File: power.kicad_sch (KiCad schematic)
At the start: 61 parts, among them J7 USB-C_GCT_USB4105-GF-A, J8 Molex_Nano-Fit_1x2_SMD_105430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, U13 TPS564247DRLR, U6 TPS564247DRLR, U7 TPS564247DRLR, U8 TPS564247DRLR, U9 TPS564247DRLR

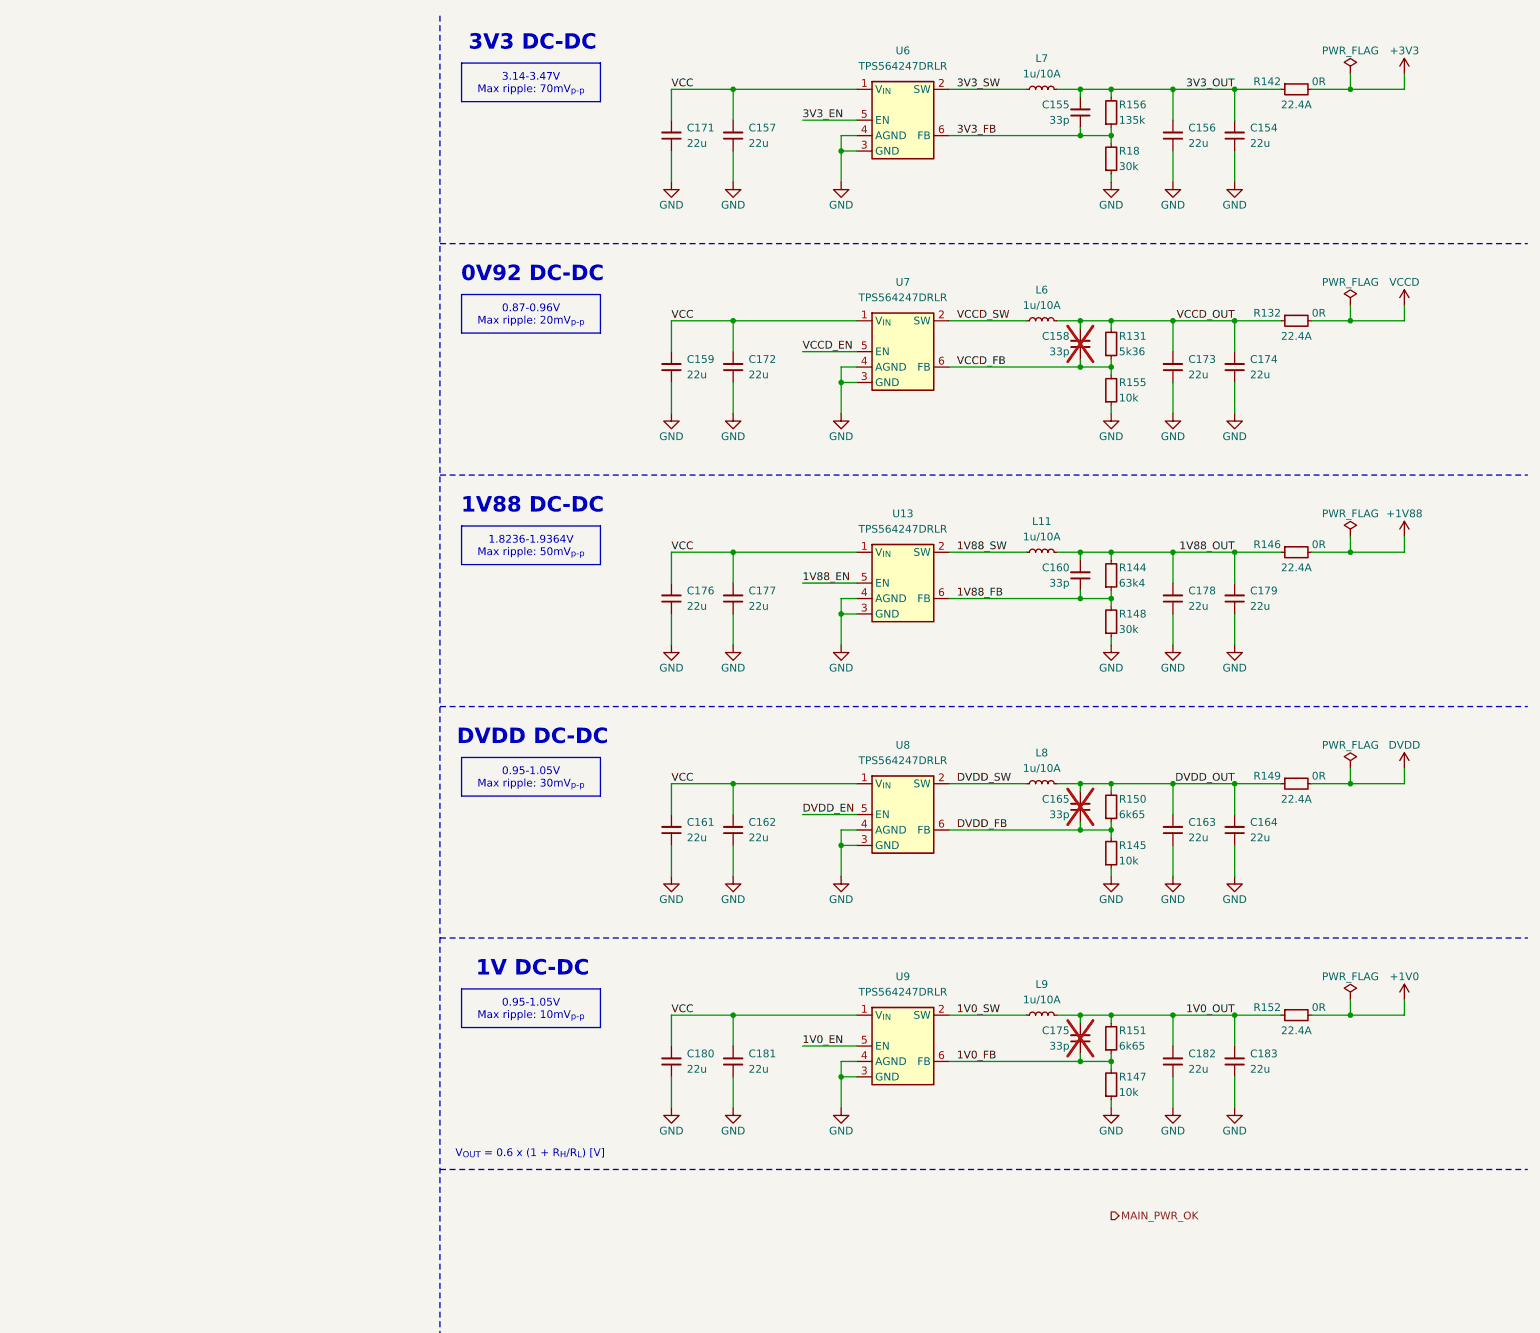
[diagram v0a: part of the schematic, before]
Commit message: [#81595] WIP: Connect remaining control signals
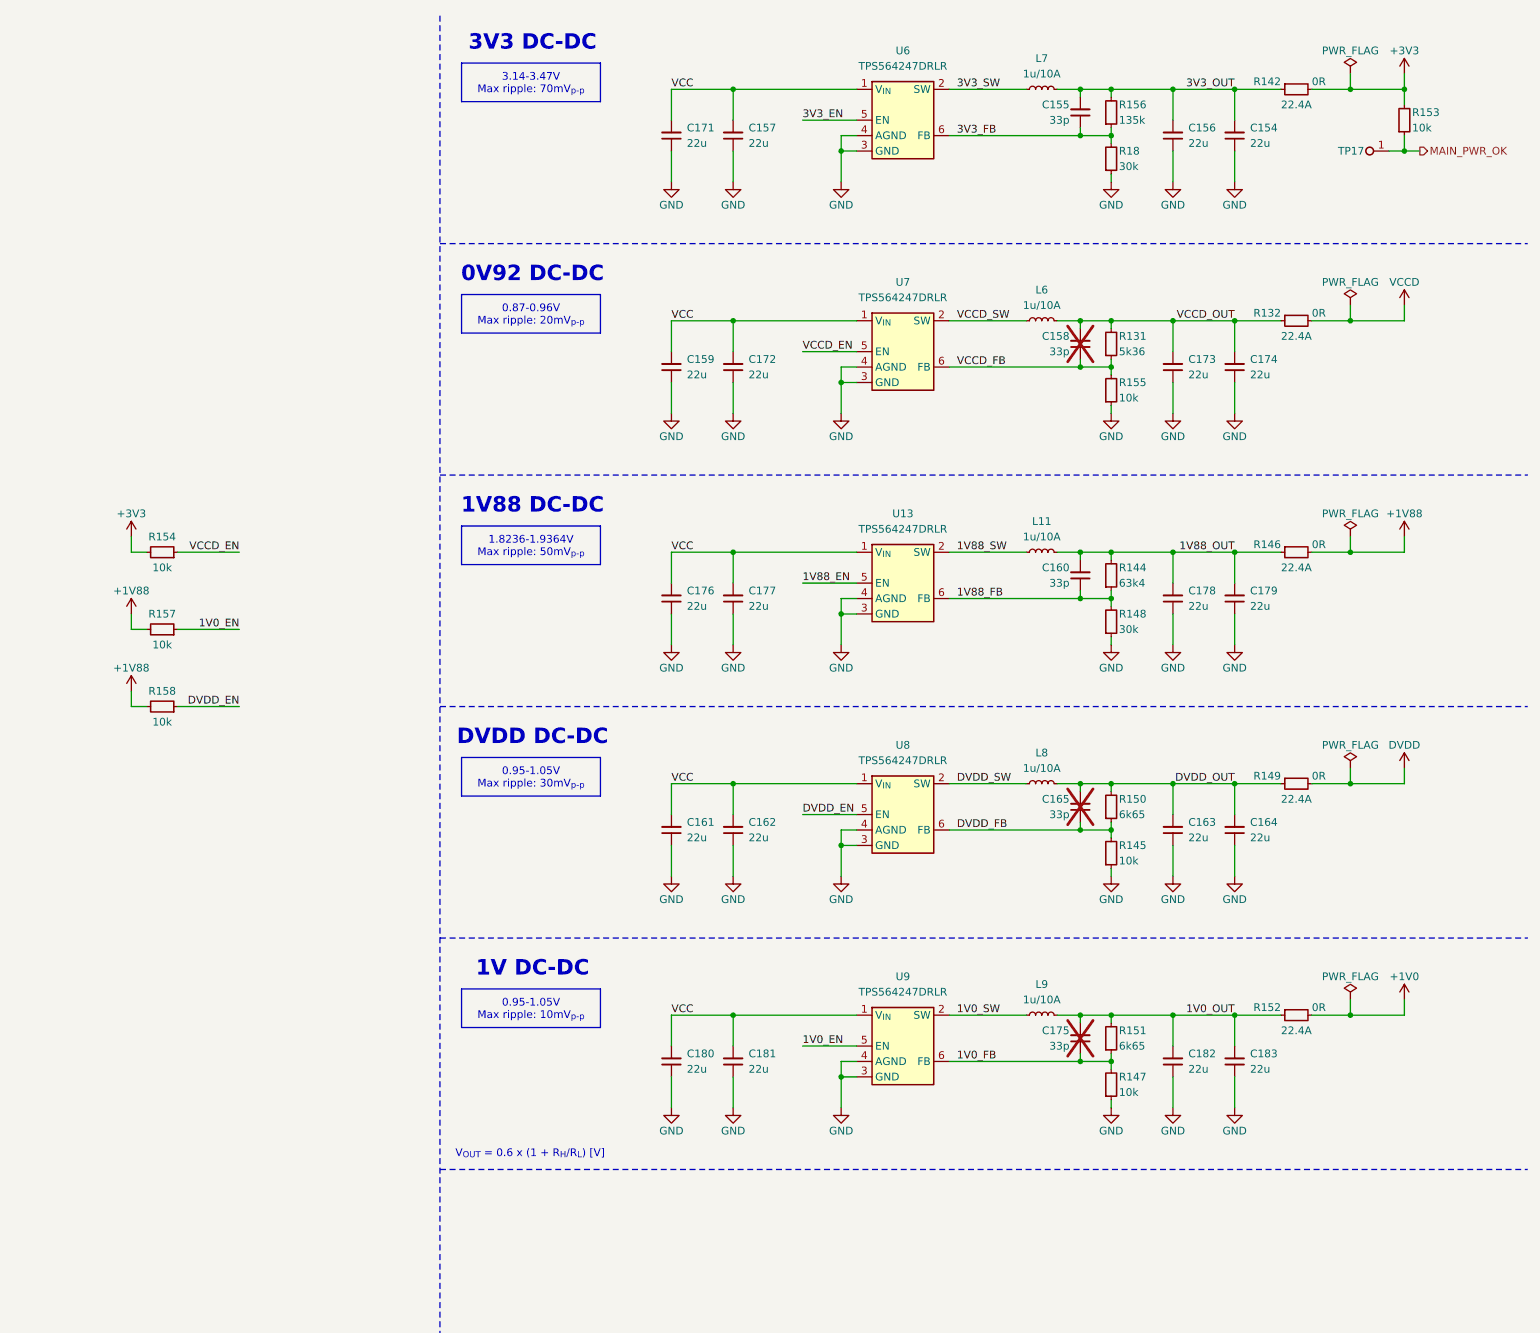
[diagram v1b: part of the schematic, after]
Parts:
- added R153, R154, R157, R158: R_10k_0402, antmicro-footprints:R_0402_1005Metric, symbol antmicroResistors0402:R_10k_0402
- added TP17: TP_0.75mm_SMD, antmicro-footprints:TP_SMD_0.75mm, symbol antmicroTestPoints:TP_0.75mm_SMD
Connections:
- net +1V88: now also R157.2, R158.2
- net +3V3: now also R153.2, R154.2
- net 1V0_EN: now also R157.1
- net DVDD_EN: now also R158.1
- net MAIN_PWR_OK: now also R153.1, TP17.1
- net VCCD_EN: now also R154.1

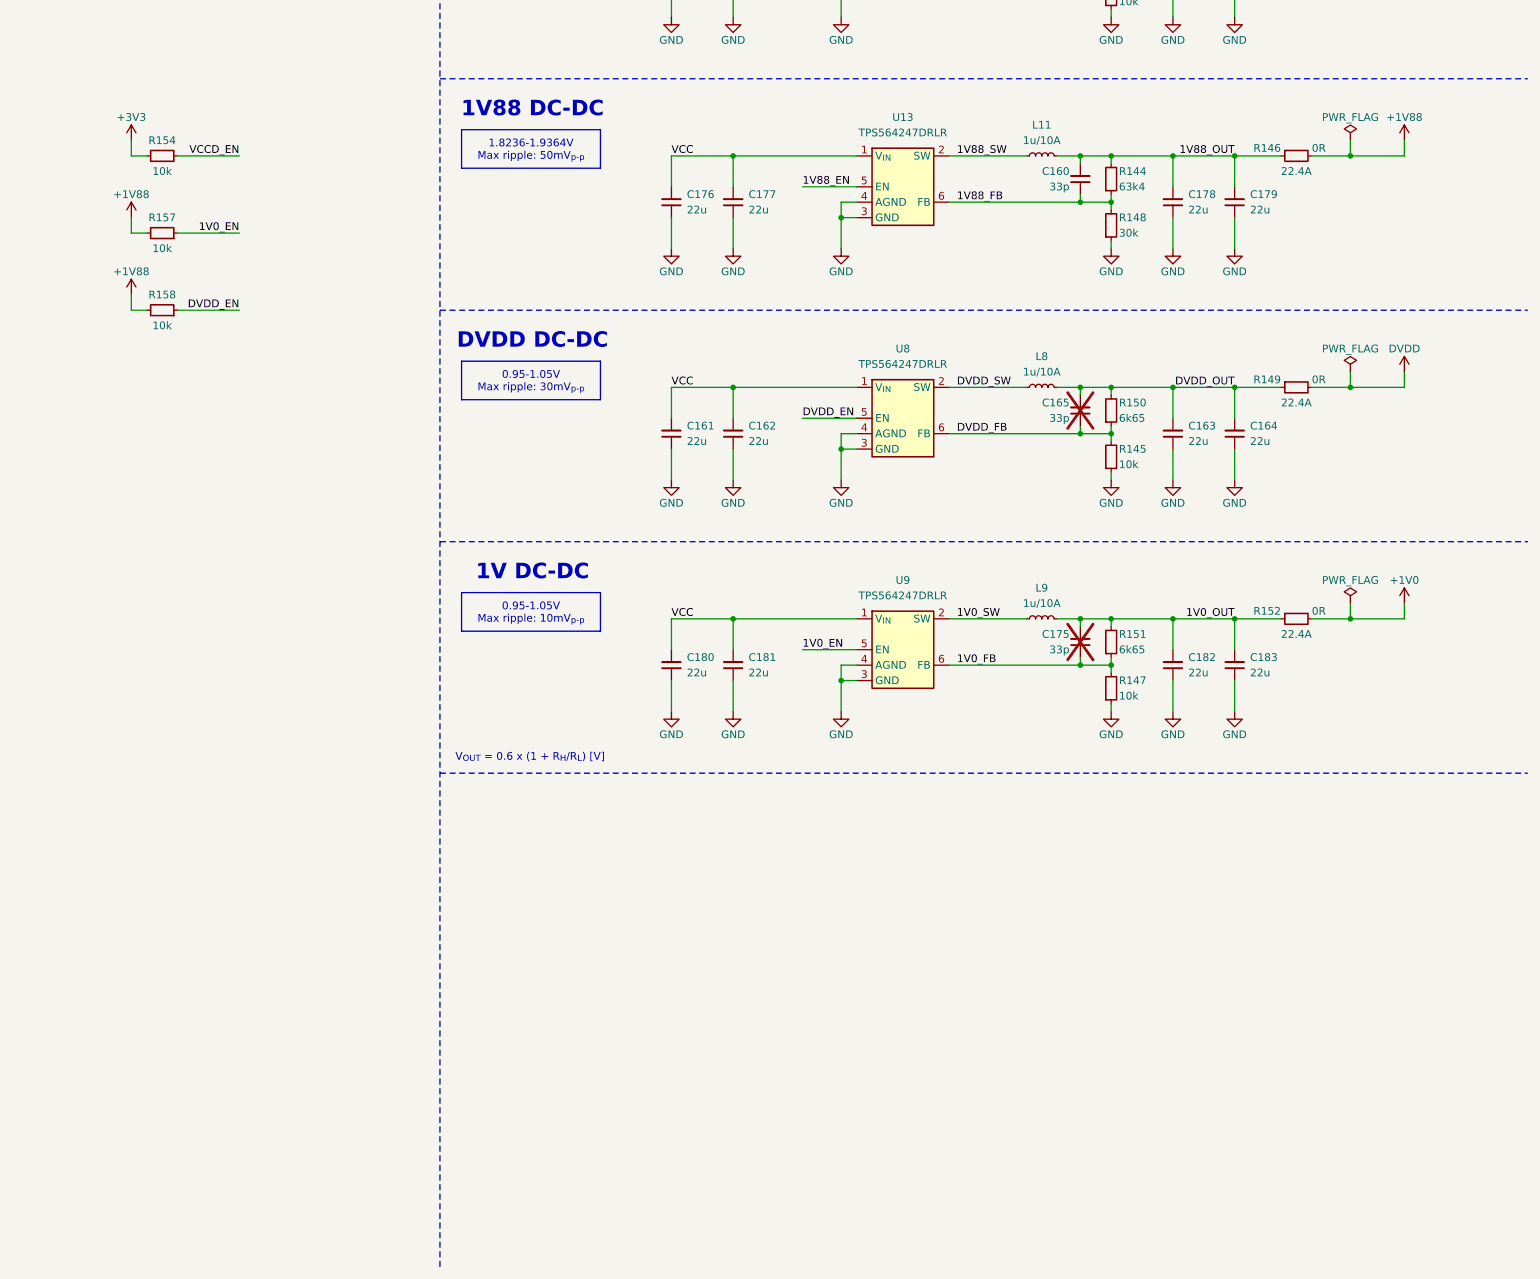
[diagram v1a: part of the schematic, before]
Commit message: [#85196] WIP: Add power sequencing, connect CPRSNT signal
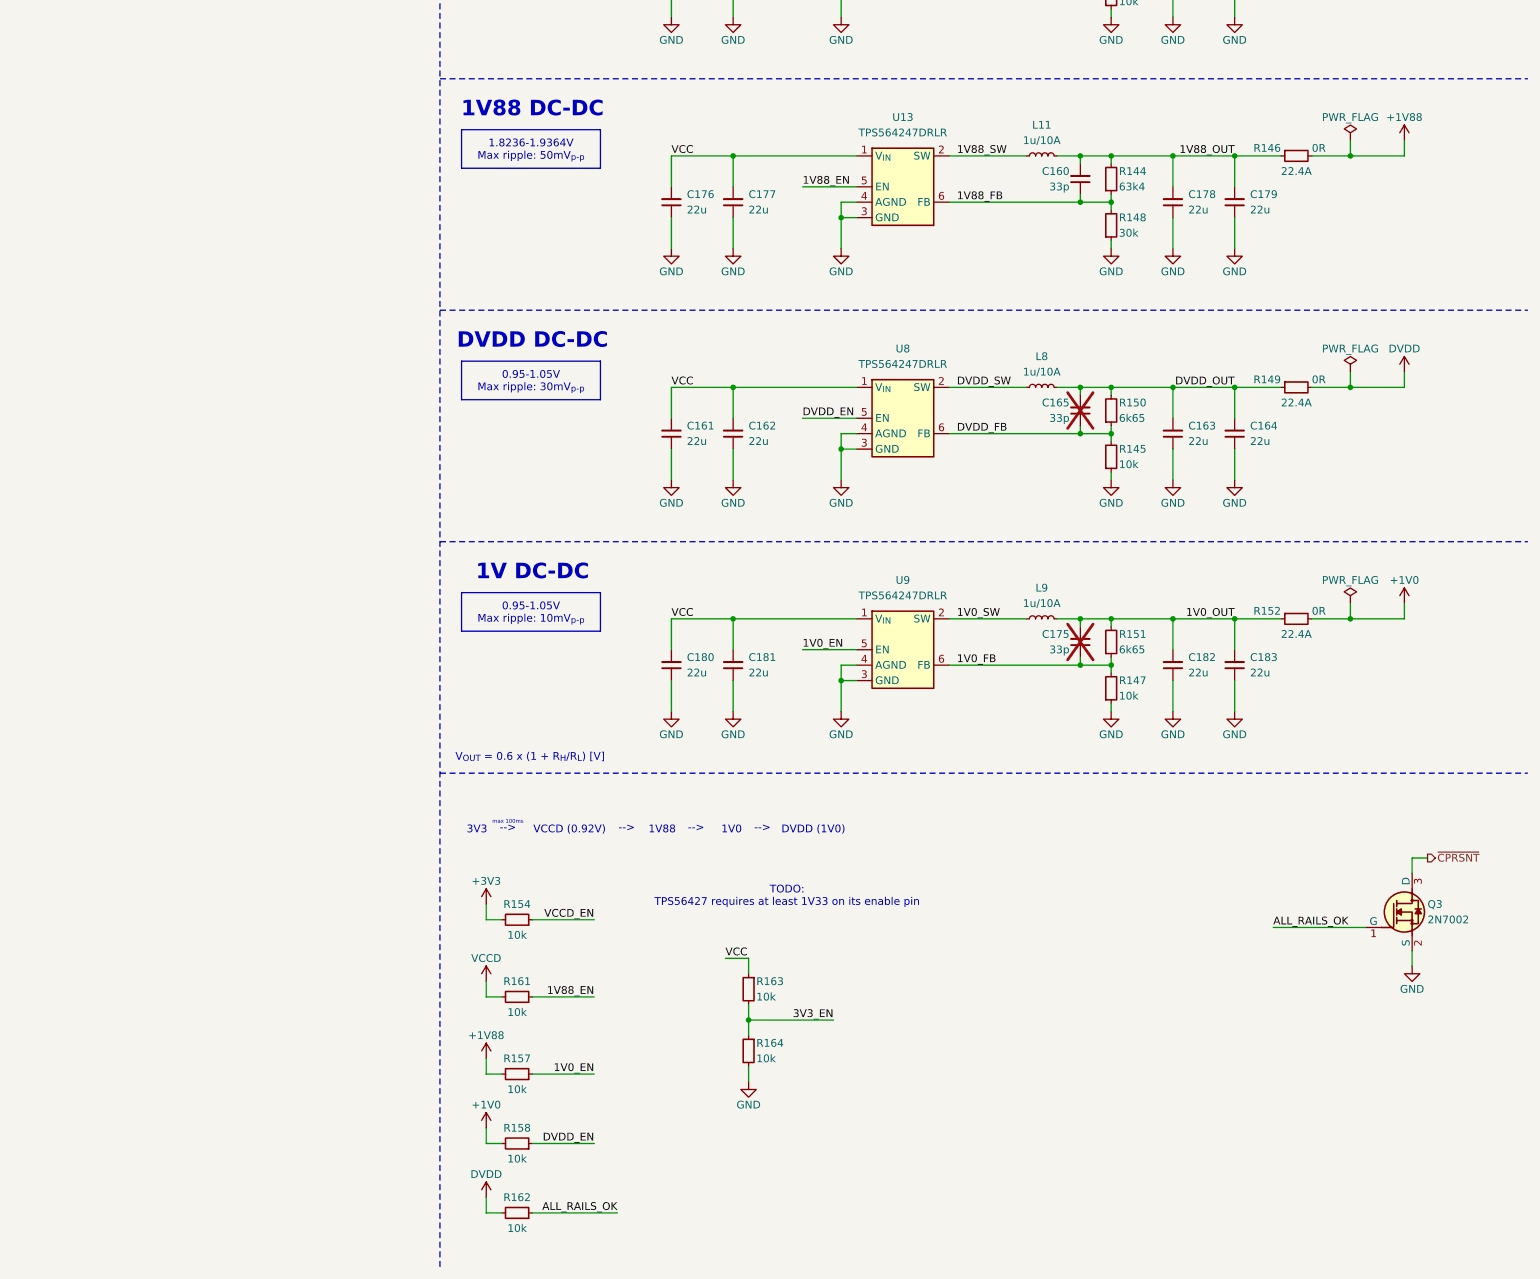
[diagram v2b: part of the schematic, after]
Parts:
- added Q3: 2N7002_SOT-23-3, antmicro-footprints:SOT-23-3, symbol antmicroTransistorsFETsMOSFETsSingle:2N7002_SOT-23-3
- added R161, R162, R163, R164: R_10k_0402, antmicro-footprints:R_0402_1005Metric, symbol antmicroResistors0402:R_10k_0402
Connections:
- net +1V0: now also R158.2
- net +1V88: no longer R158.2
- net 1V88_EN: now also R161.1
- net 3V3_EN: now also R163.2, R164.1
- net DVDD: now also R162.2
- net GND: now also Q3.2 (S), R164.2
- net VCC: now also R163.1
- net VCCD: now also R161.2
- new net ALL_RAILS_OK: Q3.1 (G), R162.1
- new net ~{CPRSNT}: Q3.3 (D)
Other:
- note added: "-->"
- note added: "1V0"
- note added: "1V88"
- note added: "3V3"
- note added: "DVDD (1V0)"
- note added: "TODO: TPS56427 requires at least 1V33 on its enable pin"
- note added: "VCCD (0.92V)"
- note added: "max 100ms"
- moved on the sheet: R154
